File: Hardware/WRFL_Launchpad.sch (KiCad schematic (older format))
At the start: 3 parts, among them P13 LAUNCHPAD_J1_J3, P14 LAUNCHPAD_J2_J4, P8 1x2_2.54_Fem

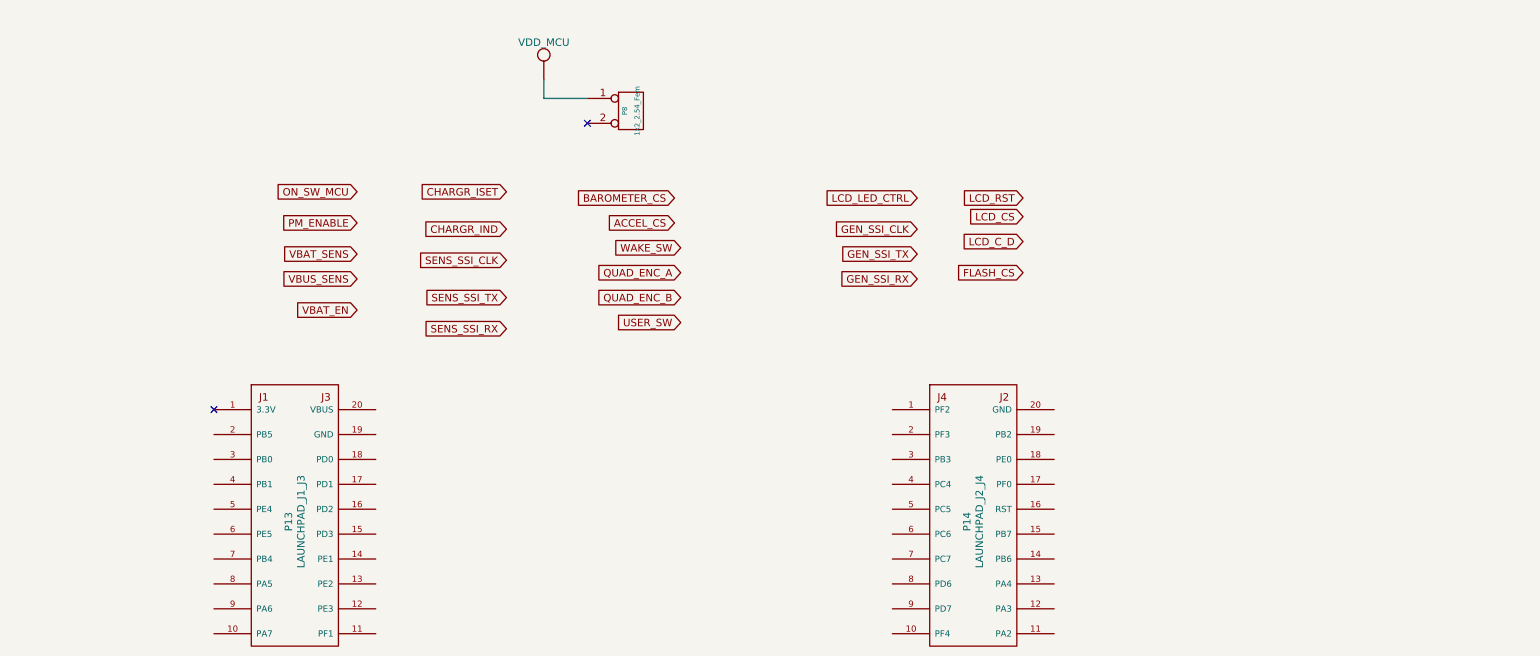
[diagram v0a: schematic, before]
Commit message: Added VREF and 2x3 for servos
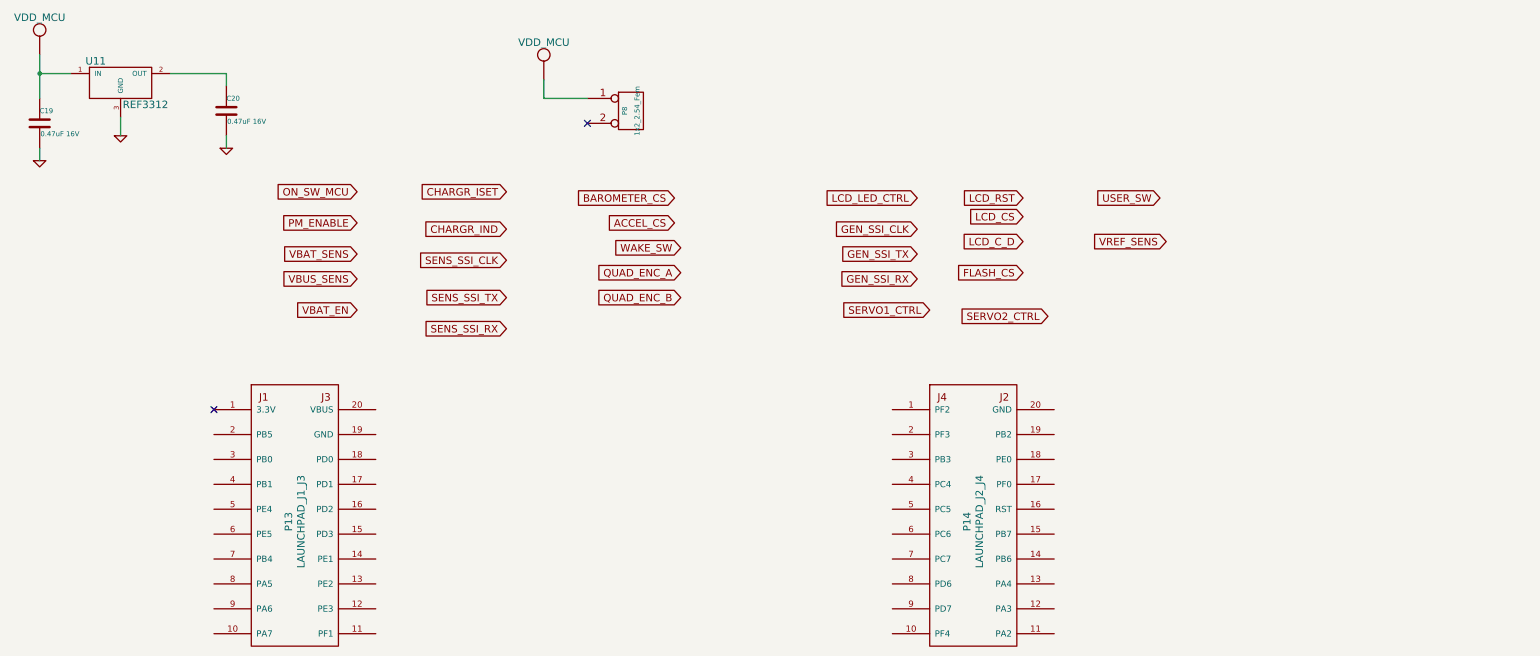
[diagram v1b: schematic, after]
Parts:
- added C19, C20: 0.47uF 16V, 0805, symbol C
- added U10: VDD_MCU, ~, symbol VDD_MCU
- added U11: REF3312, ~, symbol REF3312
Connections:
- net VDD_MCU: now also C19.1, U10.1 (VDD_MCU), U11.1 (IN)
- new net: C20.1, U11.2 (OUT)
- new net GND: C19.2, C20.2, U11.3 (GND)
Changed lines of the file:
@@
-EESchema Schematic File Version 2  date 10/7/2013 2:32:38 AM
+EESchema Schematic File Version 2  date 10/7/2013 7:37:21 AM
 LIBS:power
 LIBS:device
@@
 Sheet 3 5
 Title ""
-Date "6 oct 2013"
+Date "7 oct 2013"
 Rev ""
 Comp "Nightmechanic"
@@
 Text GLabel 6300 3050 0    60   Input ~ 0
 QUAD_ENC_B
-Text GLabel 6300 3250 0    60   Input ~ 0
+Text GLabel 10150 2250 0    60   Input ~ 0
 USER_SW
 Text GLabel 8200 2250 0    60   Input ~ 0
@@
 FLASH_CS
 NoConn ~ 2550 3950
+Text GLabel 8300 3150 0    60   Input ~ 0
+SERVO1_CTRL
+Text GLabel 9250 3200 0    60   Input ~ 0
+SERVO2_CTRL
+Text GLabel 10200 2600 0    60   Input ~ 0
+VREF_SENS
+$Comp
+L REF3312 U11
+U 1 1 525244B8
+P 1800 1300
+F 0 "U11" H 1600 1450 60  0000 C CNN
+F 1 "REF3312" H 2000 1100 60  0000 C CNN
+F 2 "~" H 1800 1300 60  0000 C CNN
+F 3 "http://www.ti.com/lit/ds/symlink/ref3312.pdf" H 1800 1650 60  0001 C CNN
+	1    1800 1300
+	1    0    0    -1
+$EndComp
+$Comp
+L C C19
+U 1 1 525246BE
+P 1150 1650
+F 0 "C19" H 1150 1750 40  0000 L CNN
+F 1 "0.47uF 16V" H 1156 1565 40  0000 L CNN
+F 2 "0805" H 1188 1500 30  0001 C CNN
+F 3 "~" H 1150 1650 60  0000 C CNN
+	1    1150 1650
+	1    0    0    -1
+$EndComp
+$Comp
+L VDD_MCU U10
+U 1 1 525246DC
+P 1150 900
+F 0 "U10" H 1150 1100 60  0001 C CNN
+F 1 "VDD_MCU" H 1150 1000 60  0000 C CNN
+F 2 "~" H 1150 900 60  0000 C CNN
+F 3 "~" H 1150 900 60  0000 C CNN
+	1    1150 900
+	1    0    0    -1
+$EndComp
+$Comp
+L GND #PWR26
+U 1 1 525246EB
+P 1150 1950
+F 0 "#PWR26" H 1150 1950 30  0001 C CNN
+F 1 "GND" H 1150 1880 30  0001 C CNN
+F 2 "" H 1150 1950 60  0000 C CNN
+F 3 "" H 1150 1950 60  0000 C CNN
+	1    1150 1950
+	1    0    0    -1
+$EndComp
+$Comp
+L GND #PWR27
+U 1 1 525246FA
+P 1800 1750
+F 0 "#PWR27" H 1800 1750 30  0001 C CNN
+F 1 "GND" H 1800 1680 30  0001 C CNN
+F 2 "" H 1800 1750 60  0000 C CNN
+F 3 "" H 1800 1750 60  0000 C CNN
+	1    1800 1750
+	1    0    0    -1
+$EndComp
+$Comp
+L GND #PWR28
+U 1 1 52524709
+P 2650 1850
+F 0 "#PWR28" H 2650 1850 30  0001 C CNN
+F 1 "GND" H 2650 1780 30  0001 C CNN
+F 2 "" H 2650 1850 60  0000 C CNN
+F 3 "" H 2650 1850 60  0000 C CNN
+	1    2650 1850
+	1    0    0    -1
+$EndComp
+Wire Wire Line
+	1150 1100 1150 1450
+Wire Wire Line
+	1150 1850 1150 1950
+Wire Wire Line
+	1400 1250 1150 1250
+Connection ~ 1150 1250
+Wire Wire Line
+	1800 1600 1800 1750
+Wire Wire Line
+	2200 1250 2650 1250
+Wire Wire Line
+	2650 1250 2650 1350
+Wire Wire Line
+	2650 1750 2650 1850
+$Comp
+L C C20
+U 1 1 52524762
+P 2650 1550
+F 0 "C20" H 2650 1650 40  0000 L CNN
+F 1 "0.47uF 16V" H 2656 1465 40  0000 L CNN
+F 2 "0805" H 2688 1400 30  0001 C CNN
+F 3 "~" H 2650 1550 60  0000 C CNN
+	1    2650 1550
+	1    0    0    -1
+$EndComp
 $EndSCHEMATC

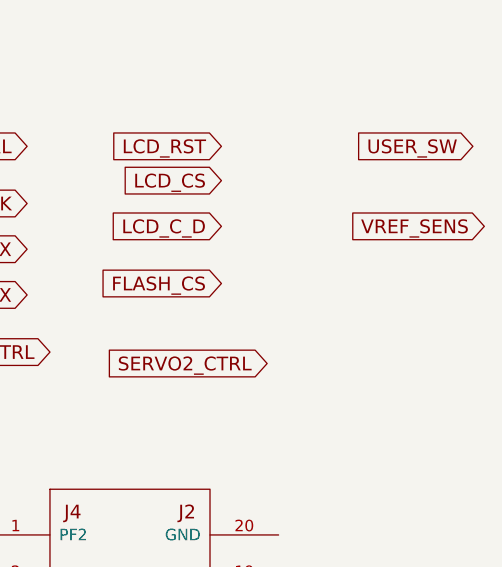
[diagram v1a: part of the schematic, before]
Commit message: Added VBAT sens
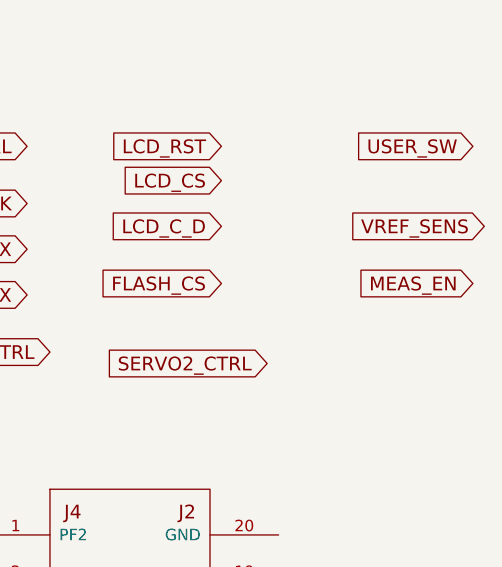
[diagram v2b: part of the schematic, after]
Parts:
- removed U10: VDD_MCU, ~, symbol VDD_MCU
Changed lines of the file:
@@
-EESchema Schematic File Version 2  date 10/7/2013 7:37:21 AM
+EESchema Schematic File Version 2  date Monday, October 07, 2013 09:14:17 AM
 LIBS:power
 LIBS:device
@@
 NoConn ~ 5550 1650
 $Comp
-L VDD_MCU #U10
+L VDD_MCU #U11
 U 1 1 524B47E3
 P 5200 1100
-F 0 "#U10" H 5200 1300 60  0001 C CNN
+F 0 "#U11" H 5200 1300 60  0001 C CNN
 F 1 "VDD_MCU" H 5200 1200 60  0000 C CNN
 F 2 "~" H 5200 1100 60  0000 C CNN
@@
 $EndComp
 $Comp
-L VDD_MCU U10
+L VDD_MCU #U10
 U 1 1 525246DC
 P 1150 900
-F 0 "U10" H 1150 1100 60  0001 C CNN
+F 0 "#U10" H 1150 1100 60  0001 C CNN
 F 1 "VDD_MCU" H 1150 1000 60  0000 C CNN
 F 2 "~" H 1150 900 60  0000 C CNN
@@
 $EndComp
 $Comp
-L GND #PWR26
+L GND #PWR28
 U 1 1 525246EB
 P 1150 1950
-F 0 "#PWR26" H 1150 1950 30  0001 C CNN
+F 0 "#PWR28" H 1150 1950 30  0001 C CNN
 F 1 "GND" H 1150 1880 30  0001 C CNN
 F 2 "" H 1150 1950 60  0000 C CNN
@@
 $EndComp
 $Comp
-L GND #PWR27
+L GND #PWR29
 U 1 1 525246FA
 P 1800 1750
-F 0 "#PWR27" H 1800 1750 30  0001 C CNN
+F 0 "#PWR29" H 1800 1750 30  0001 C CNN
 F 1 "GND" H 1800 1680 30  0001 C CNN
 F 2 "" H 1800 1750 60  0000 C CNN
@@
 $EndComp
 $Comp
-L GND #PWR28
+L GND #PWR30
 U 1 1 52524709
 P 2650 1850
-F 0 "#PWR28" H 2650 1850 30  0001 C CNN
+F 0 "#PWR30" H 2650 1850 30  0001 C CNN
 F 1 "GND" H 2650 1780 30  0001 C CNN
 F 2 "" H 2650 1850 60  0000 C CNN
@@
 	1    0    0    -1
 $EndComp
+Text GLabel 10150 2850 0    60   Input ~ 0
+MEAS_EN
 $EndSCHEMATC

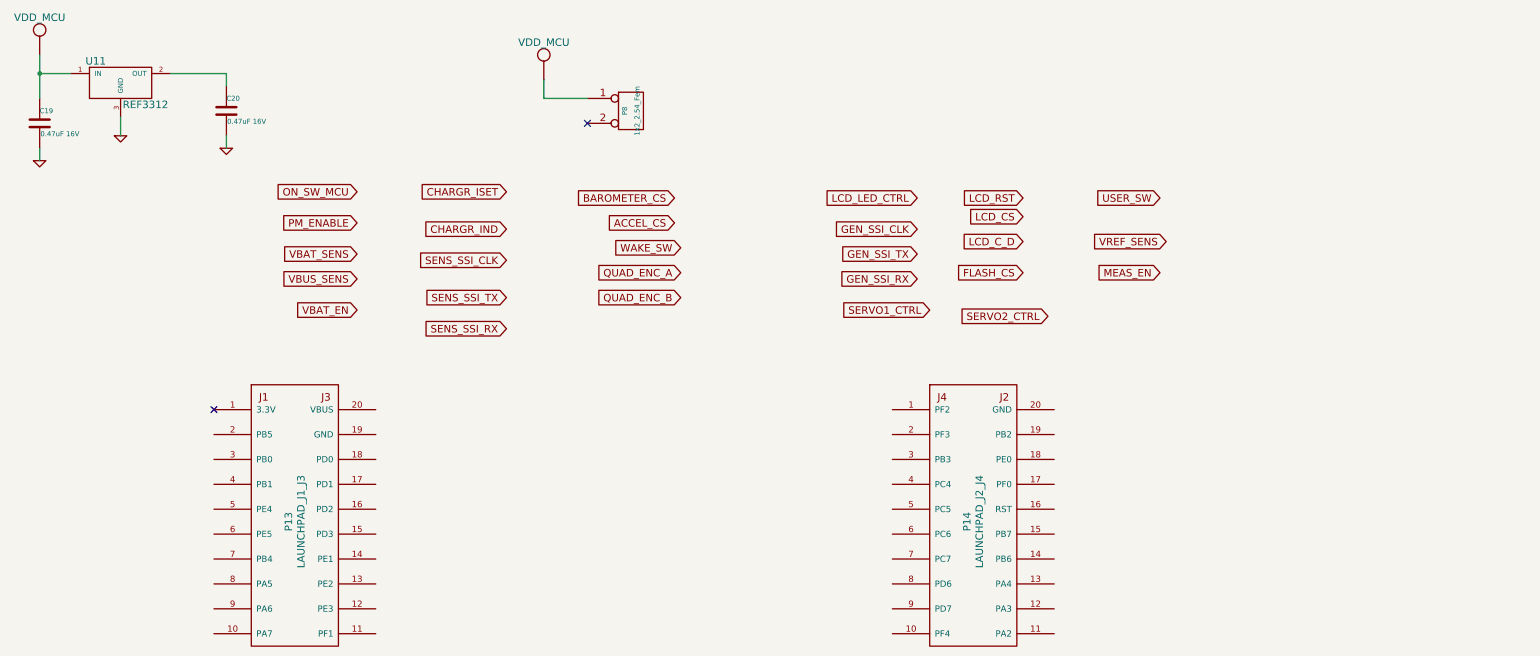
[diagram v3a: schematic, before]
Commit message: Schematics update
Bluetooth sheet added
LCD specific symbol
power management sheet rearrangement
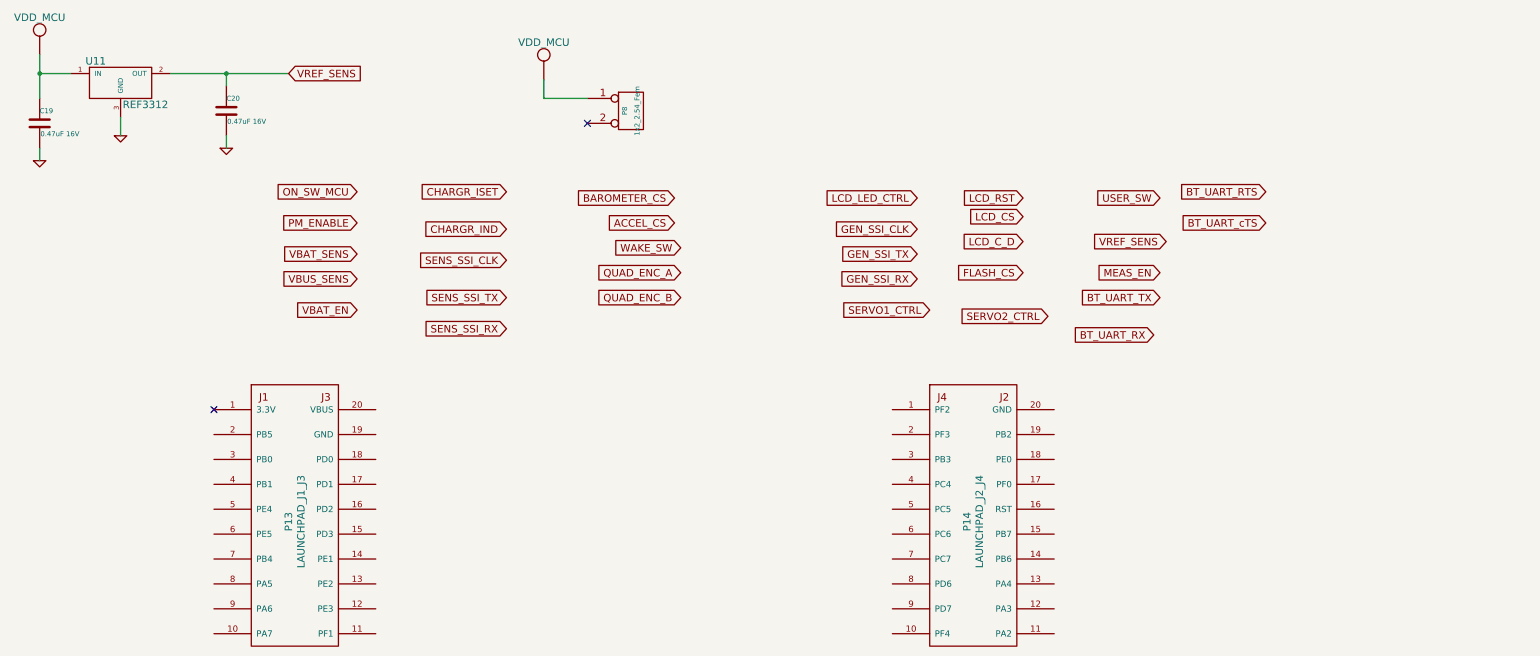
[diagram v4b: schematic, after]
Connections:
- net VREF_SENS: now also C20.1, U11.2 (OUT)
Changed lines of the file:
@@
-EESchema Schematic File Version 2  date Monday, October 07, 2013 12:52:48 PM
+EESchema Schematic File Version 2  date 10/11/2013 1:57:23 AM
 LIBS:power
 LIBS:device
@@
 $Descr A4 11693 8268
 encoding utf-8
-Sheet 3 5
+Sheet 3 6
 Title ""
-Date "7 oct 2013"
+Date "10 oct 2013"
 Rev ""
 Comp "Nightmechanic"
@@
 NoConn ~ 5550 1650
 $Comp
-L VDD_MCU #U11
+L VDD_MCU #U12
 U 1 1 524B47E3
 P 5200 1100
-F 0 "#U11" H 5200 1300 60  0001 C CNN
+F 0 "#U12" H 5200 1300 60  0001 C CNN
 F 1 "VDD_MCU" H 5200 1200 60  0000 C CNN
 F 2 "~" H 5200 1100 60  0000 C CNN
@@
 $EndComp
 $Comp
-L VDD_MCU #U10
+L VDD_MCU #U11
 U 1 1 525246DC
 P 1150 900
-F 0 "#U10" H 1150 1100 60  0001 C CNN
+F 0 "#U11" H 1150 1100 60  0001 C CNN
 F 1 "VDD_MCU" H 1150 1000 60  0000 C CNN
 F 2 "~" H 1150 900 60  0000 C CNN
@@
 	1800 1600 1800 1750
 Wire Wire Line
-	2200 1250 2650 1250
+	2200 1250 3150 1250
 Wire Wire Line
 	2650 1250 2650 1350
@@
 Text GLabel 10150 2850 0    60   Input ~ 0
 MEAS_EN
+Text GLabel 10150 3050 0    60   Input ~ 0
+BT_UART_TX
+Text GLabel 10100 3350 0    60   Input ~ 0
+BT_UART_RX
+Text GLabel 11000 2200 0    60   Input ~ 0
+BT_UART_RTS
+Text GLabel 11000 2450 0    60   Input ~ 0
+BT_UART_cTS
+Text GLabel 3150 1250 2    60   Input ~ 0
+VREF_SENS
+Connection ~ 2650 1250
 $EndSCHEMATC
